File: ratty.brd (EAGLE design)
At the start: 616 x 652 mm, 87 parts, among them IC2 L293DD, Q1 MOSFET-NCHANNELBSS123LT1G, Q2 MOSFET-NCHANNELBSS123LT1G, Q3 MOSFET-NCHANNELBSS123LT1G, Q5 MOSFET-NCHANNELBSS123LT1G, U1 ITG-32001:1

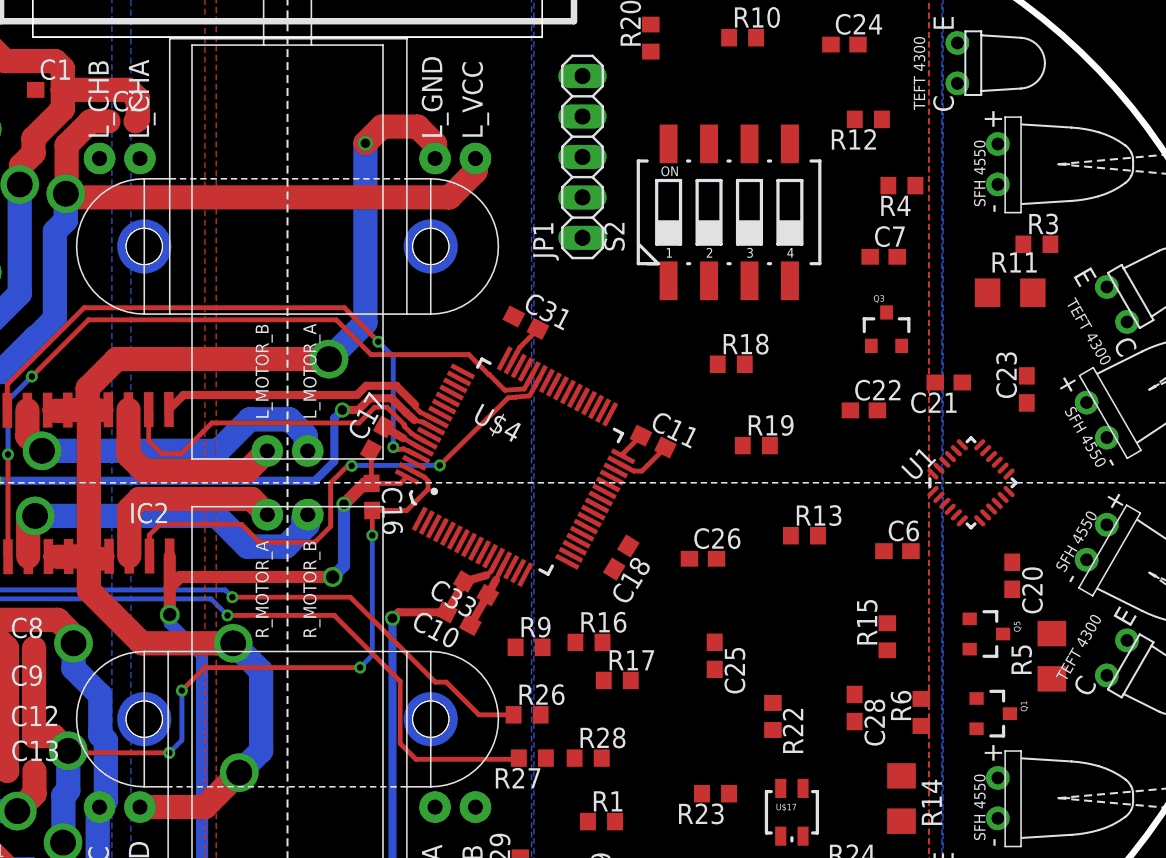
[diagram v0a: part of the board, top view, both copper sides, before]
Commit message: Routed gyro
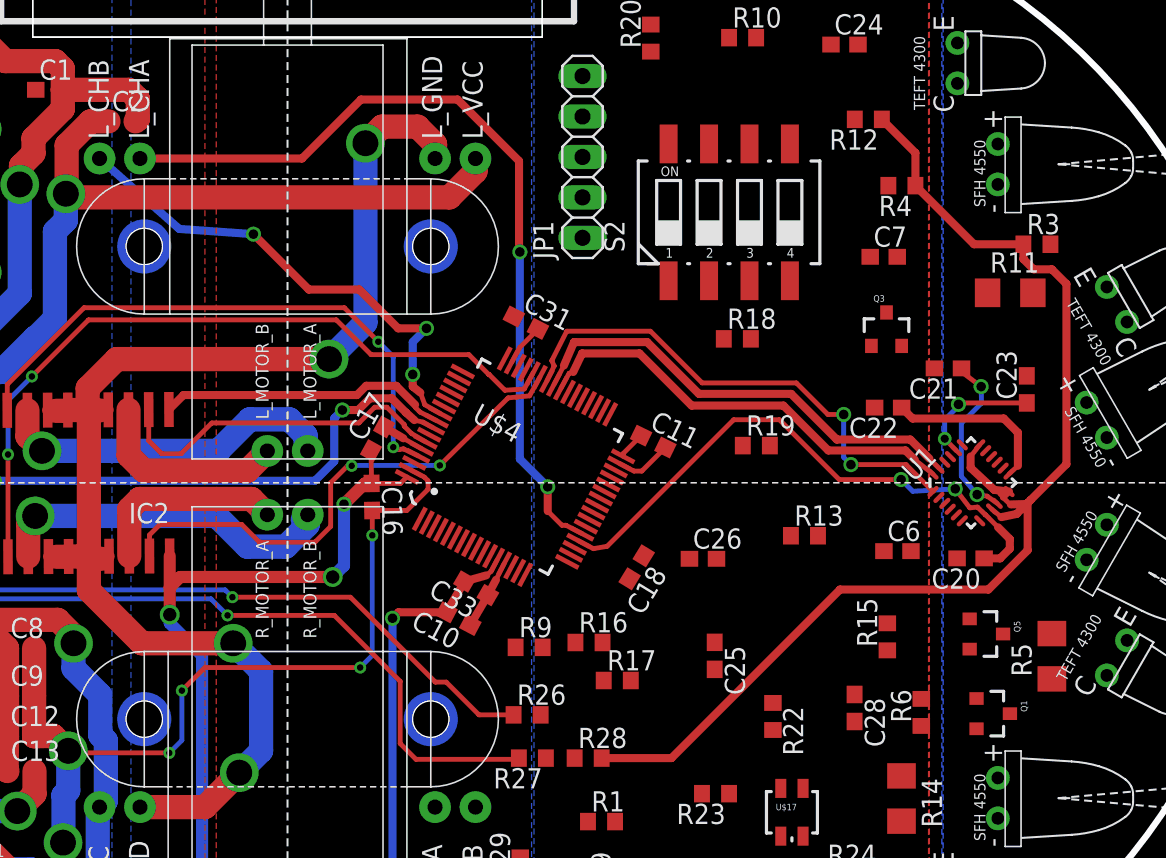
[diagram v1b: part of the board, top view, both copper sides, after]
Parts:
- moved C20 2.84 mm to (68.9, 32.5), turned to 180 degrees
- moved R18 1.64 mm to (54.3, 46.3)
- moved C22 1.53 mm to (63.7, 42.0), turned to 180 degrees
- moved C18 1.14 mm to (47.9, 31.9)
- moved C21 0.89 mm to (67.5, 44.4)
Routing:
- net AGND: track 53.0 -> 130.1 mm
- net ENCODER1_1: track 0.00 -> 52.4 mm, vias 0 -> 2
- net GYROVLOGIC: track 0.00 -> 36.3 mm, vias 0 -> 2
- net GYROCLK: track 0.00 -> 32.2 mm, vias 0 -> 2
- net ENCODER1_2: track 0.00 -> 31.2 mm, vias 0 -> 3
- net I2CSCL_FOR_GYRO: track 0.00 -> 29.2 mm
- net I2CSDA_FOR_GYRO: track 0.00 -> 27.8 mm
- net GYROREGOUT: track 0.00 -> 10.9 mm, vias 0 -> 2
- net 3.3V: track 74.5 -> 85.3 mm
- net GYROCPOUT: track 0.00 -> 7.87 mm, vias 0 -> 2

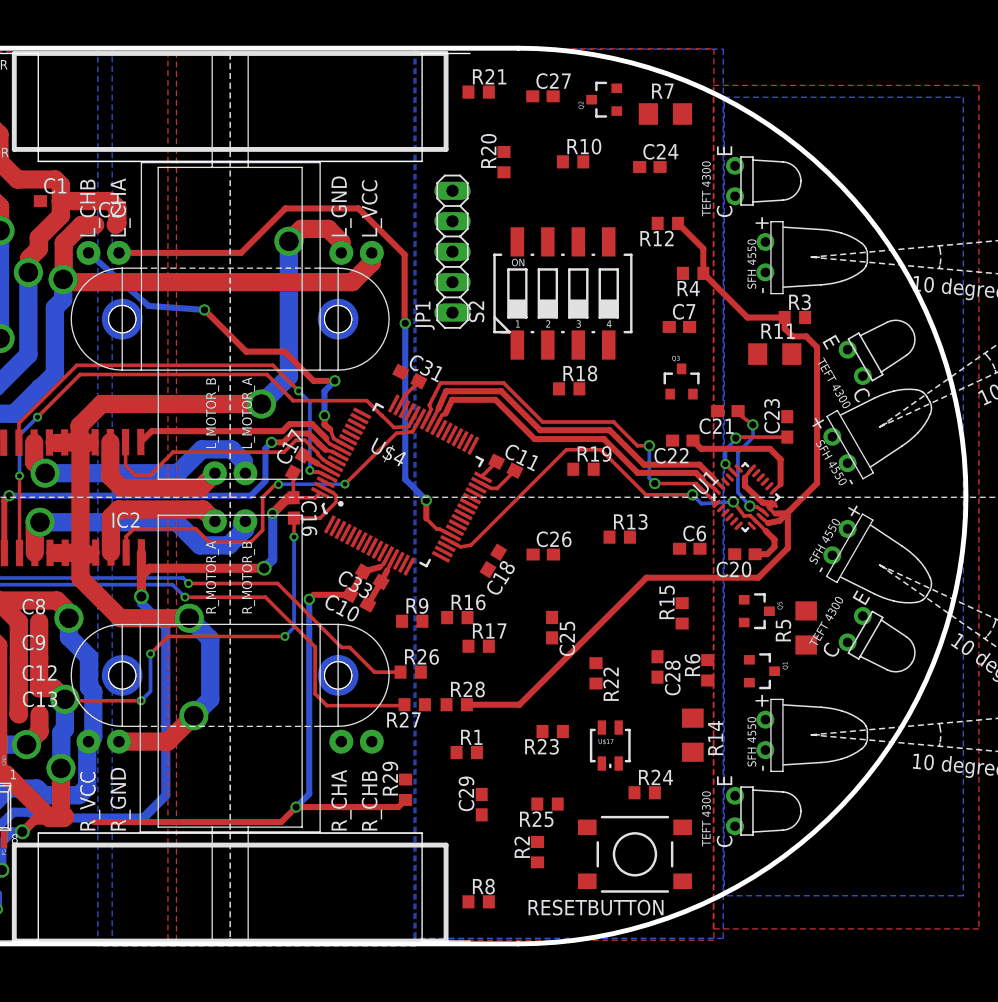
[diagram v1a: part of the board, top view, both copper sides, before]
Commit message: routed right and thinngs to the outside and working my way in
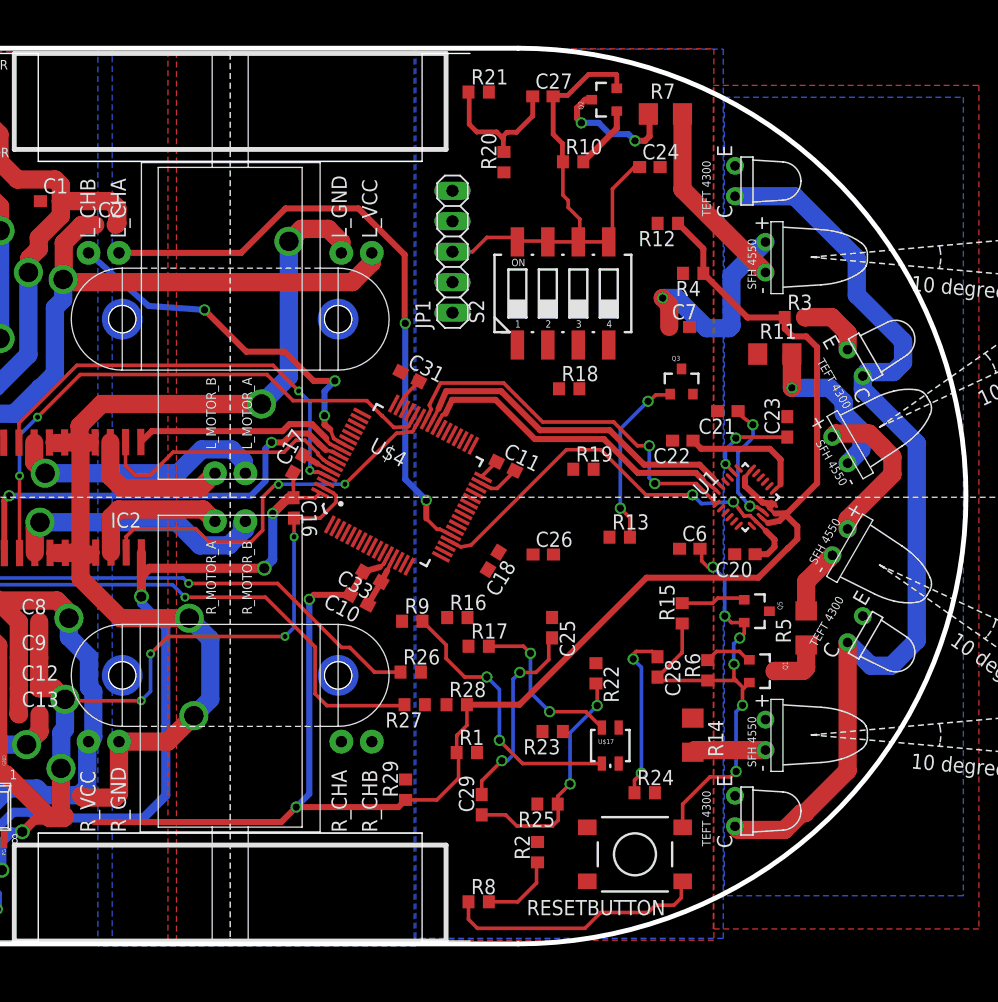
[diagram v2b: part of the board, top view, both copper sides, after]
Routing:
- net DGND: track 79.4 -> 179.6 mm, vias 8 -> 16
- net 3.3V_NUCLEO: track 0.00 -> 80.0 mm
- net 5V: track 119.0 -> 150.1 mm, vias 4 -> 5
- net N$18: track 0.00 -> 23.0 mm, vias 0 -> 2
- net NRST_CIRCUIT_MCU: track 0.00 -> 22.0 mm
- net TO_R22/C29: track 0.00 -> 19.8 mm, vias 0 -> 2
- net LED/R7: track 0.00 -> 16.1 mm
- net PB_0_EMIT_CIRCUIT_3: track 0.00 -> 14.7 mm, vias 0 -> 2
- net TO_R19/C28: track 0.00 -> 14.4 mm, vias 0 -> 2
- net N$20: track 0.00 -> 14.2 mm, vias 0 -> 2
- net LED/R11: track 0.00 -> 13.8 mm, vias 0 -> 1
- net AGND: track 130.1 -> 142.3 mm
- net TO_R20/C27: track 0.00 -> 12.2 mm
- net TO_Q2_MOS: track 0.00 -> 11.3 mm, vias 0 -> 2
- net MGND: track 84.1 -> 91.8 mm
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
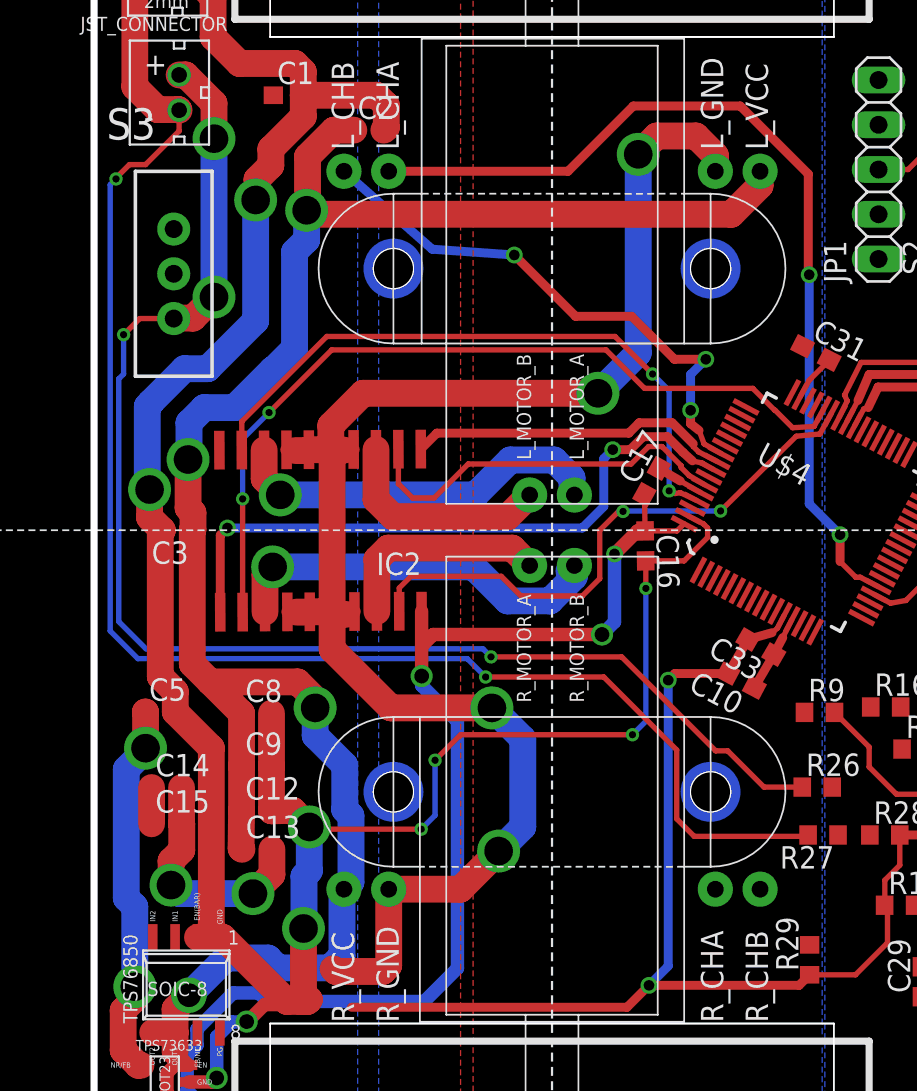
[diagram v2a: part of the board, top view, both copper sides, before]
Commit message: Fixed widths of some power routes
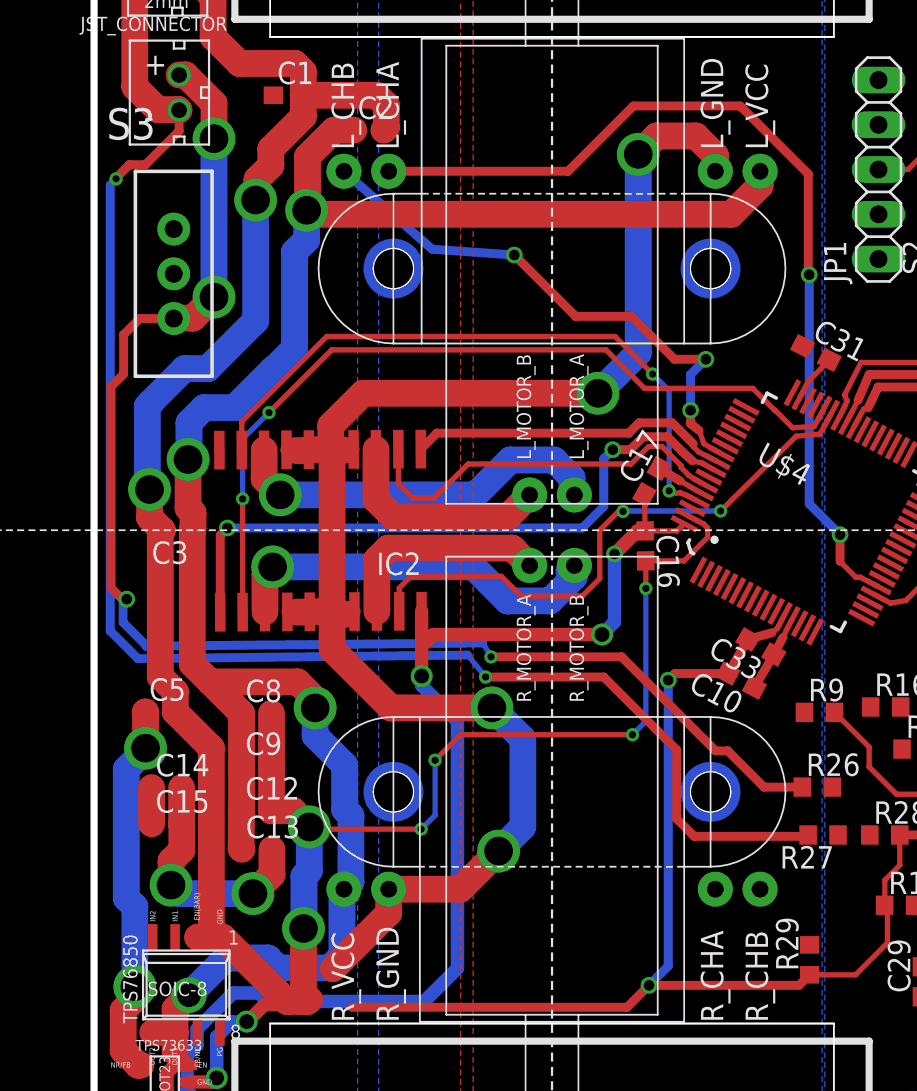
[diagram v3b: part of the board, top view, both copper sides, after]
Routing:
- net MGND: track 91.8 -> 89.9 mm
- net BATTERY_1: track 78.7 -> 79.5 mm
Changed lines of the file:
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@@
 <?xml version="1.0" encoding="utf-8"?>
 <!DOCTYPE eagle SYSTEM "eagle.dtd">
-<eagle version="7.5.0">
+<eagle version="7.7.0">
 <drawing>
 <settings>
@@
 <wire x1="3.6068" y1="61.1124" x2="4.7912" y2="61.1124" width="1.524" layer="1"/>
 <wire x1="4.7912" y1="61.1124" x2="4.826" y2="61.0776" width="1.524" layer="1"/>
-<wire x1="4.826" y1="61.0776" x2="4.826" y2="59.8932" width="0.3048" layer="1"/>
-<wire x1="4.826" y1="59.8932" x2="2.921" y2="57.9882" width="0.3048" layer="1"/>
-<wire x1="2.921" y1="57.9882" x2="2.0066" y2="57.9882" width="0.3048" layer="1"/>
-<wire x1="0.9144" y1="31.5214" x2="2.4892" y2="29.9466" width="0.3048" layer="16"/>
-<wire x1="2.4892" y1="29.9466" x2="21.1836" y2="29.9466" width="0.3048" layer="16"/>
-<wire x1="21.1836" y1="29.9466" x2="22.225" y2="28.9052" width="0.3048" layer="16"/>
+<wire x1="4.826" y1="61.0776" x2="4.826" y2="59.8932" width="0.508" layer="1"/>
+<wire x1="4.826" y1="59.8932" x2="2.921" y2="57.9882" width="0.508" layer="1"/>
+<wire x1="2.921" y1="57.9882" x2="2.0066" y2="57.9882" width="0.508" layer="1"/>
+<wire x1="0.9144" y1="31.5214" x2="2.4892" y2="29.9466" width="0.508" layer="16"/>
+<wire x1="2.4892" y1="29.9466" x2="21.209" y2="30.1498" width="0.508" layer="16"/>
+<wire x1="21.209" y1="30.1498" x2="22.225" y2="28.9052" width="0.3048" layer="16"/>
 <via x="22.225" y="28.9052" extent="1-16" drill="0.4064"/>
-<wire x1="22.225" y1="28.9052" x2="28.9306" y2="28.9052" width="0.3048" layer="1"/>
-<wire x1="28.9306" y1="28.9052" x2="33.0708" y2="24.765" width="0.3048" layer="1"/>
-<wire x1="33.0708" y1="24.765" x2="33.0708" y2="20.8534" width="0.3048" layer="1"/>
-<wire x1="33.0708" y1="20.8534" x2="34.0614" y2="19.8628" width="0.3048" layer="1"/>
-<wire x1="34.0614" y1="19.8628" x2="40.4504" y2="19.8628" width="0.3048" layer="1"/>
+<wire x1="22.225" y1="28.9052" x2="28.9306" y2="28.9052" width="0.508" layer="1"/>
+<wire x1="28.9306" y1="28.9052" x2="33.0708" y2="24.765" width="0.508" layer="1"/>
+<wire x1="33.0708" y1="24.765" x2="33.0708" y2="20.8534" width="0.508" layer="1"/>
+<wire x1="33.0708" y1="20.8534" x2="34.0614" y2="19.8628" width="0.508" layer="1"/>
+<wire x1="34.0614" y1="19.8628" x2="40.4504" y2="19.8628" width="0.508" layer="1"/>
 <wire x1="40.4504" y1="19.8628" x2="40.5266" y2="19.939" width="0.3048" layer="1"/>
-<wire x1="0.9144" y1="56.8452" x2="0.9144" y2="31.5214" width="0.3048" layer="16"/>
+<wire x1="0.9144" y1="56.8452" x2="0.9144" y2="31.5214" width="0.508" layer="16"/>
 <wire x1="0.9144" y1="56.8452" x2="1.2446" y2="57.1754" width="0.3048" layer="16"/>
 <via x="1.2446" y="57.1754" extent="1-16" drill="0.4064"/>
 <wire x1="1.2446" y1="57.1754" x2="1.2446" y2="57.2262" width="0.3048" layer="1"/>
-<wire x1="1.2446" y1="57.2262" x2="2.0066" y2="57.9882" width="0.3048" layer="1"/>
+<wire x1="1.2446" y1="57.2262" x2="2.0066" y2="57.9882" width="0.508" layer="1"/>
 </signal>
 <signal name="GND">
@@
 <wire x1="5.6134" y1="49.276" x2="4.5466" y2="49.276" width="1.524" layer="1"/>
 <wire x1="4.5466" y1="49.276" x2="4.5212" y2="49.2506" width="1.524" layer="1"/>
-<wire x1="4.5212" y1="49.2506" x2="2.5908" y2="49.2506" width="0.3048" layer="1"/>
-<wire x1="1.397" y1="32.0548" x2="2.9464" y2="30.5054" width="0.3048" layer="16"/>
-<wire x1="2.9464" y1="30.5054" x2="22.0726" y2="30.5054" width="0.3048" layer="16"/>
-<wire x1="22.0726" y1="30.5054" x2="22.5298" y2="30.0482" width="0.3048" layer="16"/>
+<wire x1="4.5212" y1="49.2506" x2="2.5908" y2="49.2506" width="0.508" layer="1"/>
+<wire x1="2.9464" y1="30.6578" x2="22.0726" y2="30.8356" width="0.508" layer="16"/>
+<wire x1="22.0726" y1="30.8356" x2="22.5298" y2="30.0482" width="0.3048" layer="16"/>
 <via x="22.5298" y="30.0482" extent="1-16" drill="0.4064"/>
-<wire x1="22.5298" y1="30.0482" x2="29.9466" y2="30.0482" width="0.3048" layer="1"/>
-<wire x1="29.9466" y1="30.0482" x2="35.2806" y2="24.7142" width="0.3048" layer="1"/>
-<wire x1="2.5908" y1="49.2506" x2="1.6764" y2="48.3362" width="0.3048" layer="1"/>
-<via x="1.6764" y="48.3362" extent="1-16" drill="0.4064"/>
-<wire x1="1.6764" y1="48.3362" x2="1.6764" y2="46.101" width="0.3048" layer="16"/>
-<wire x1="1.6764" y1="46.101" x2="1.397" y2="45.8216" width="0.3048" layer="16"/>
-<wire x1="1.397" y1="45.8216" x2="1.397" y2="32.0548" width="0.3048" layer="16"/>
-<wire x1="35.2806" y1="24.7142" x2="35.9664" y2="24.7142" width="0.3048" layer="1"/>
-<wire x1="35.9664" y1="24.7142" x2="38.0238" y2="22.6568" width="0.3048" layer="1"/>
-<wire x1="38.0238" y1="22.6568" x2="40.1964" y2="22.6568" width="0.3048" layer="1"/>
+<wire x1="22.5298" y1="30.0482" x2="29.9466" y2="30.0482" width="0.508" layer="1"/>
+<wire x1="29.9466" y1="30.0482" x2="35.2806" y2="24.7142" width="0.508" layer="1"/>
+<wire x1="2.5908" y1="49.2506" x2="1.6764" y2="48.3362" width="0.508" layer="1"/>
+<wire x1="1.6764" y1="48.3362" x2="1.6764" y2="46.101" width="0.508" layer="1"/>
+<wire x1="35.2806" y1="24.7142" x2="35.9664" y2="24.7142" width="0.508" layer="1"/>
+<wire x1="35.9664" y1="24.7142" x2="38.0238" y2="22.6568" width="0.508" layer="1"/>
+<wire x1="38.0238" y1="22.6568" x2="40.1964" y2="22.6568" width="0.508" layer="1"/>
+<wire x1="1.6764" y1="46.101" x2="0.9652" y2="45.3898" width="0.508" layer="1"/>
+<wire x1="0.9652" y1="45.3898" x2="0.9652" y2="33.9598" width="0.508" layer="1"/>
+<wire x1="0.9652" y1="33.9598" x2="1.6002" y2="33.3248" width="0.508" layer="1"/>
+<wire x1="1.6002" y1="33.3248" x2="1.8542" y2="33.3248" width="0.508" layer="1"/>
+<via x="1.8542" y="33.3248" extent="1-16" drill="0.6"/>
+<wire x1="1.8542" y1="33.3248" x2="1.651" y2="33.1216" width="0.508" layer="16"/>
+<wire x1="1.651" y1="33.1216" x2="1.651" y2="32.004" width="0.508" layer="16"/>
+<wire x1="1.651" y1="32.004" x2="2.9464" y2="30.7086" width="0.508" layer="16"/>
+<wire x1="2.9464" y1="30.7086" x2="2.9464" y2="30.6578" width="0.508" layer="16"/>
 </signal>
 <signal name="BATTERY">
@@
 <vertex x="0.1016" y="0.1016"/>
 </polygon>
+<wire x1="4.5974" y1="14.13" x2="7.113390625" y2="41.7810125" width="0" layer="19" extent="1-1"/>
 </signal>
 <signal name="L_DIGITAL_IN_2">
@@
 <wire x1="13.4366" y1="43.18" x2="13.4366" y2="41.8409625" width="1.524" layer="1"/>
 <wire x1="13.4366" y1="41.8409625" x2="13.463303125" y2="41.814259375" width="1.524" layer="1"/>
-<wire x1="16.7224" y1="16.8614" x2="16.7224" y2="12.5314" width="1.524" layer="1"/>
-<wire x1="16.7224" y1="12.5314" x2="16.383" y2="12.192" width="1.524" layer="1"/>
-<wire x1="16.383" y1="12.192" x2="13.716" y2="12.192" width="1.524" layer="1"/>
-<wire x1="13.716" y1="12.192" x2="13.5636" y2="12.3444" width="1.524" layer="1"/>
+<wire x1="16.7224" y1="16.8614" x2="16.7224" y2="15.5032" width="1.524" layer="1"/>
+<wire x1="16.7224" y1="15.5032" x2="13.5636" y2="12.3444" width="1.524" layer="1"/>
 </signal>
 <signal name="DGND">
